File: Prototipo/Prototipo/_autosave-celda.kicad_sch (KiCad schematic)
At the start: 13 parts, among them Q11_1 MMBT2222A, Q11_2 MMBT2907A, Q11_3 MMBT2222A

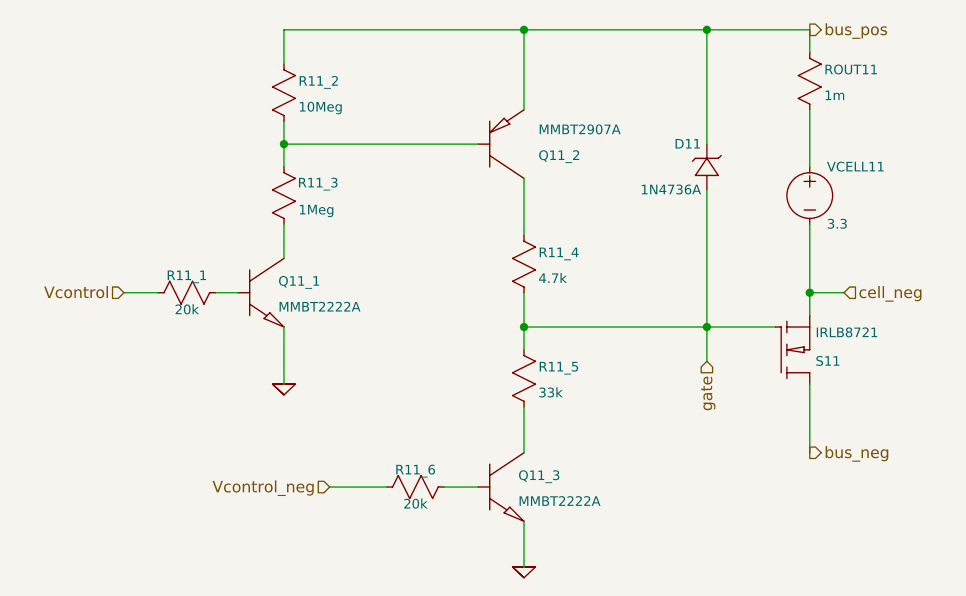
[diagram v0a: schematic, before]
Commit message: propuesta de disposición de los elementos del pcb
subo antes de empezar a hacer el ruteo
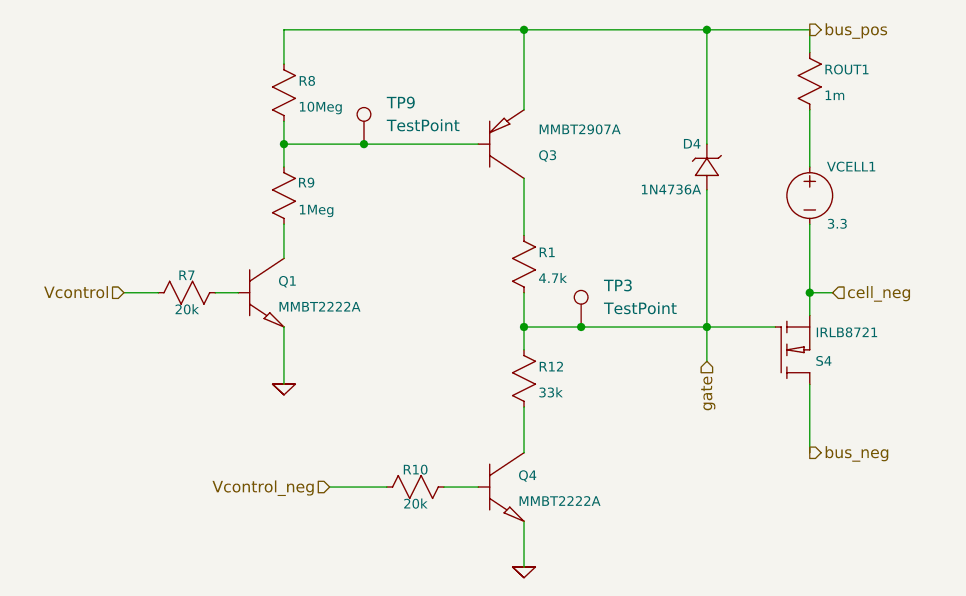
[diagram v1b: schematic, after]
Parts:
- added TP3, TP9: TestPoint, TestPoint:TestPoint_Bridge_Pitch2.54mm_Drill1.0mm, symbol Connector:TestPoint
- renumbered D11 to D4, Q11_1 to Q1, Q11_2 to Q3, Q11_3 to Q4, R11_4 to R1, R11_6 to R10, R11_5 to R12, R11_1 to R7, R11_2 to R8, R11_3 to R9, ROUT11 to ROUT1, S11 to S4, VCELL11 to VCELL1
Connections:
- net gate: now also TP3.1
- net at Q3.1 (B), R8.2, R9.1: now also TP9.1
